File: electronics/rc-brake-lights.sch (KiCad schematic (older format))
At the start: 8 parts, among them J1 TH, J2 LED, U1 STC15x10x

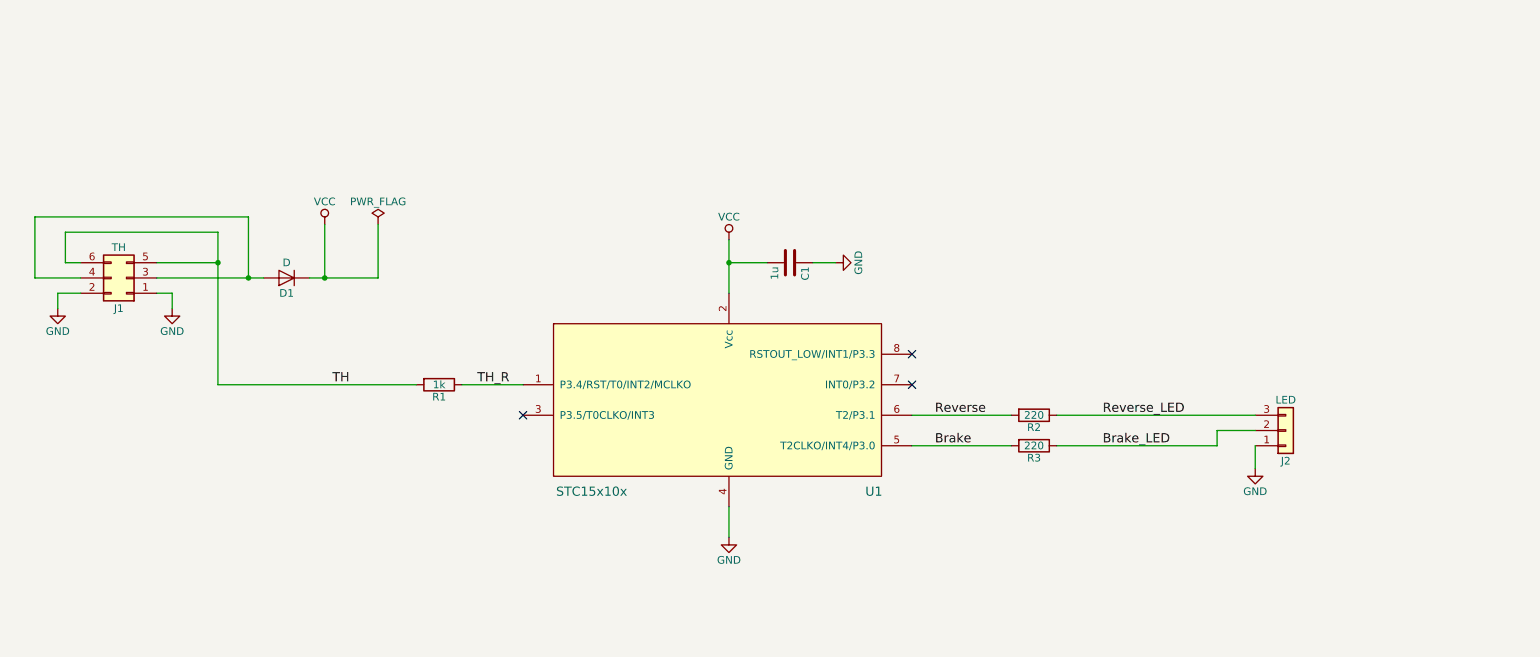
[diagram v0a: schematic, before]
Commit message: Move IO pins so we can use T0 to measure pulse width
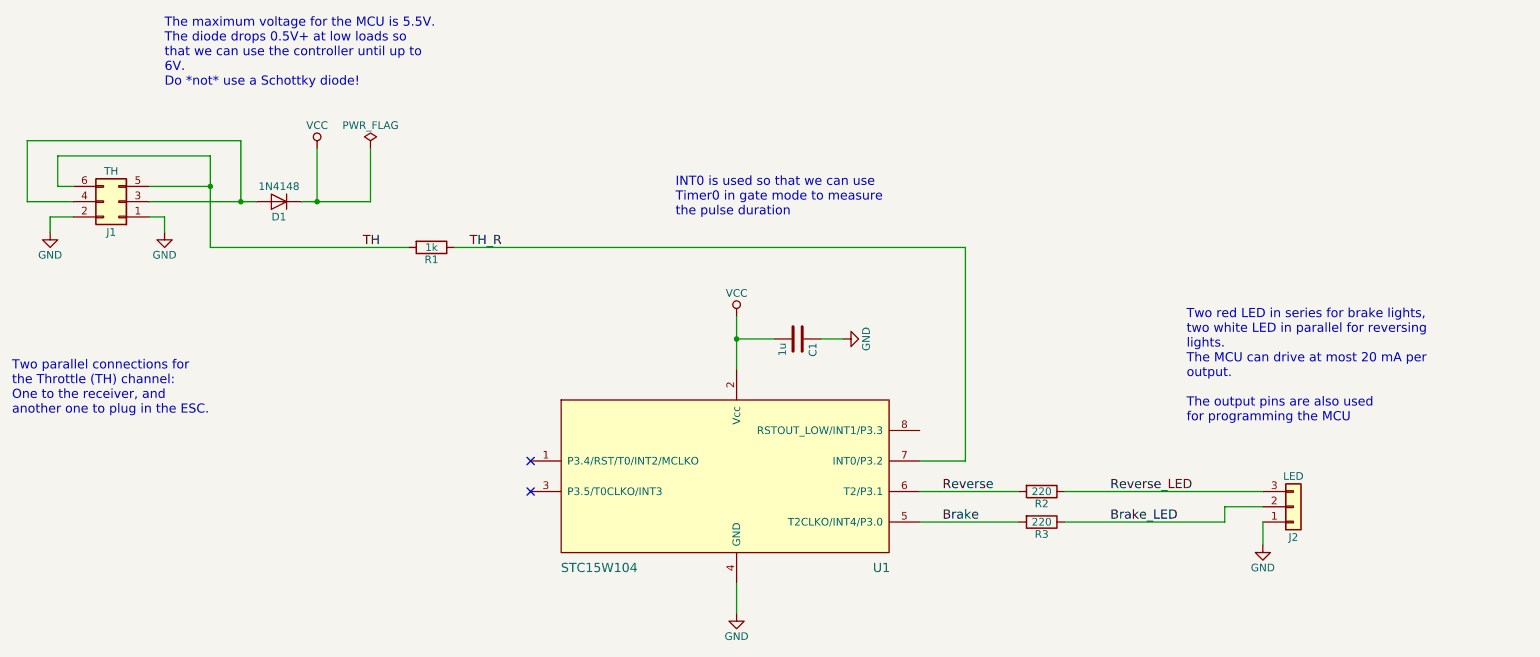
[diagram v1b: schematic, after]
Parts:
- D1: value D -> 1N4148
- U1: value STC15x10x -> STC15W104
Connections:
- net TH_R: now also U1.7 (INT0/P3.2); no longer U1.1 (P3.4/RST/T0/INT2/MCLKO)
- no-connect marks 3 -> 2
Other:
- note added: "INT0 is used so that we can use \nTimer0 in gate mode to measure\nthe pulse duration"
- note added: "The maximum voltage for the MCU is 5.5V.\nThe diode drops 0.5V+ at low loads so\nthat we can use the controller until up to\n6V. \nDo *not* use a Schottky diode!"
- note added: "Two parallel connections for \nthe Throttle (TH) channel:\nOne to the receiver, and \nanother one to plug in the ESC."
- note added: "Two red LED in series for brake lights,\ntwo white LED in parallel for reversing \nlights.\nThe MCU can drive at most 20 mA per \noutput.\n\nThe output pins are also used \nfor programming the MCU"
- moved on the sheet: C1, D1, J1, J2, R1, R2, R3, U1

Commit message: Add setup button
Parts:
- added SW1: Setup button, WLA:Tact_switch_SMD_6x3_6x2_5, symbol SW_Push
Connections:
- net GND: now also SW1.1
- net at U1.3 (P3.5/T0CLKO/INT3): now also SW1.2
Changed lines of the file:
@@
 Wire Wire Line
 	5950 5200 5950 5400
-NoConn ~ 4600 4600
 Wire Wire Line
 	6650 3600 6500 3600
@@
 Wire Wire Line
 	7150 4600 7800 4600
+Wire Wire Line
+	3900 4600 4600 4600
+$Comp
+L GND #PWR09
+U 1 1 5AC0AD67
+P 3300 4750
+F 0 "#PWR09" H 3300 4500 50  0001 C CNN
+F 1 "GND" H 3300 4600 50  0000 C CNN
+F 2 "" H 3300 4750 50  0001 C CNN
+F 3 "" H 3300 4750 50  0001 C CNN
+	1    3300 4750
+	1    0    0    -1
+$EndComp
+Wire Wire Line
+	3500 4600 3300 4600
+$Comp
+L SW_Push SW1
+U 1 1 5AC0AC8B
+P 3700 4600
+F 0 "SW1" H 3750 4700 50  0000 L CNN
+F 1 "Setup button" H 3700 4540 50  0000 C CNN
+F 2 "WLA:Tact_switch_SMD_6x3_6x2_5" H 3700 4800 50  0001 C CNN
+F 3 "" H 3700 4800 50  0001 C CNN
+	1    3700 4600
+	1    0    0    -1
+$EndComp
+NoConn ~ 7150 4200
+$Comp
+L PWR_FLAG #FLG010
+U 1 1 5AC0C3FE
+P 4250 2350
+F 0 "#FLG010" H 4250 2425 50  0001 C CNN
+F 1 "PWR_FLAG" H 4250 2500 50  0000 C CNN
+F 2 "" H 4250 2350 50  0001 C CNN
+F 3 "" H 4250 2350 50  0001 C CNN
+	1    4250 2350
+	1    0    0    -1
+$EndComp
+$Comp
+L GND #PWR011
+U 1 1 5AC0C424
+P 4250 2450
+F 0 "#PWR011" H 4250 2200 50  0001 C CNN
+F 1 "GND" H 4250 2300 50  0000 C CNN
+F 2 "" H 4250 2450 50  0001 C CNN
+F 3 "" H 4250 2450 50  0001 C CNN
+	1    4250 2450
+	1    0    0    -1
+$EndComp
+Wire Wire Line
+	4250 2350 4250 2450
+Wire Wire Line
+	3300 4600 3300 4750
 $EndSCHEMATC

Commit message: Make output connector right-angle
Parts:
- C1: value 1u -> 10u
- J2: footprint Pin_Headers:Pin_Header_Straight_1x03_Pitch2.54mm -> Pin_Headers:Pin_Header_Angled_1x03_Pitch2.54mm
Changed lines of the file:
@@
 F 0 "J2" H 9600 4900 50  0000 C CNN
 F 1 "LED" H 9600 4500 50  0000 C CNN
-F 2 "Pin_Headers:Pin_Header_Straight_1x03_Pitch2.54mm" H 9600 4700 50  0001 C CNN
+F 2 "Pin_Headers:Pin_Header_Angled_1x03_Pitch2.54mm" H 9600 4700 50  0001 C CNN
 F 3 "" H 9600 4700 50  0001 C CNN
 	1    9600 4700
@@
 P 6350 3600
 F 0 "C1" H 6375 3700 50  0000 L CNN
-F 1 "1u" H 6375 3500 50  0000 L CNN
+F 1 "10u" H 6375 3500 50  0000 L CNN
 F 2 "Capacitors_SMD:C_0603_HandSoldering" H 6388 3450 50  0001 C CNN
 F 3 "" H 6350 3600 50  0001 C CNN
